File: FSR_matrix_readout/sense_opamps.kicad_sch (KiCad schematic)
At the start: 24 parts, among them U18 TLV9064, U19 TLV9064, U20 TLV9064, U3 TLV9064

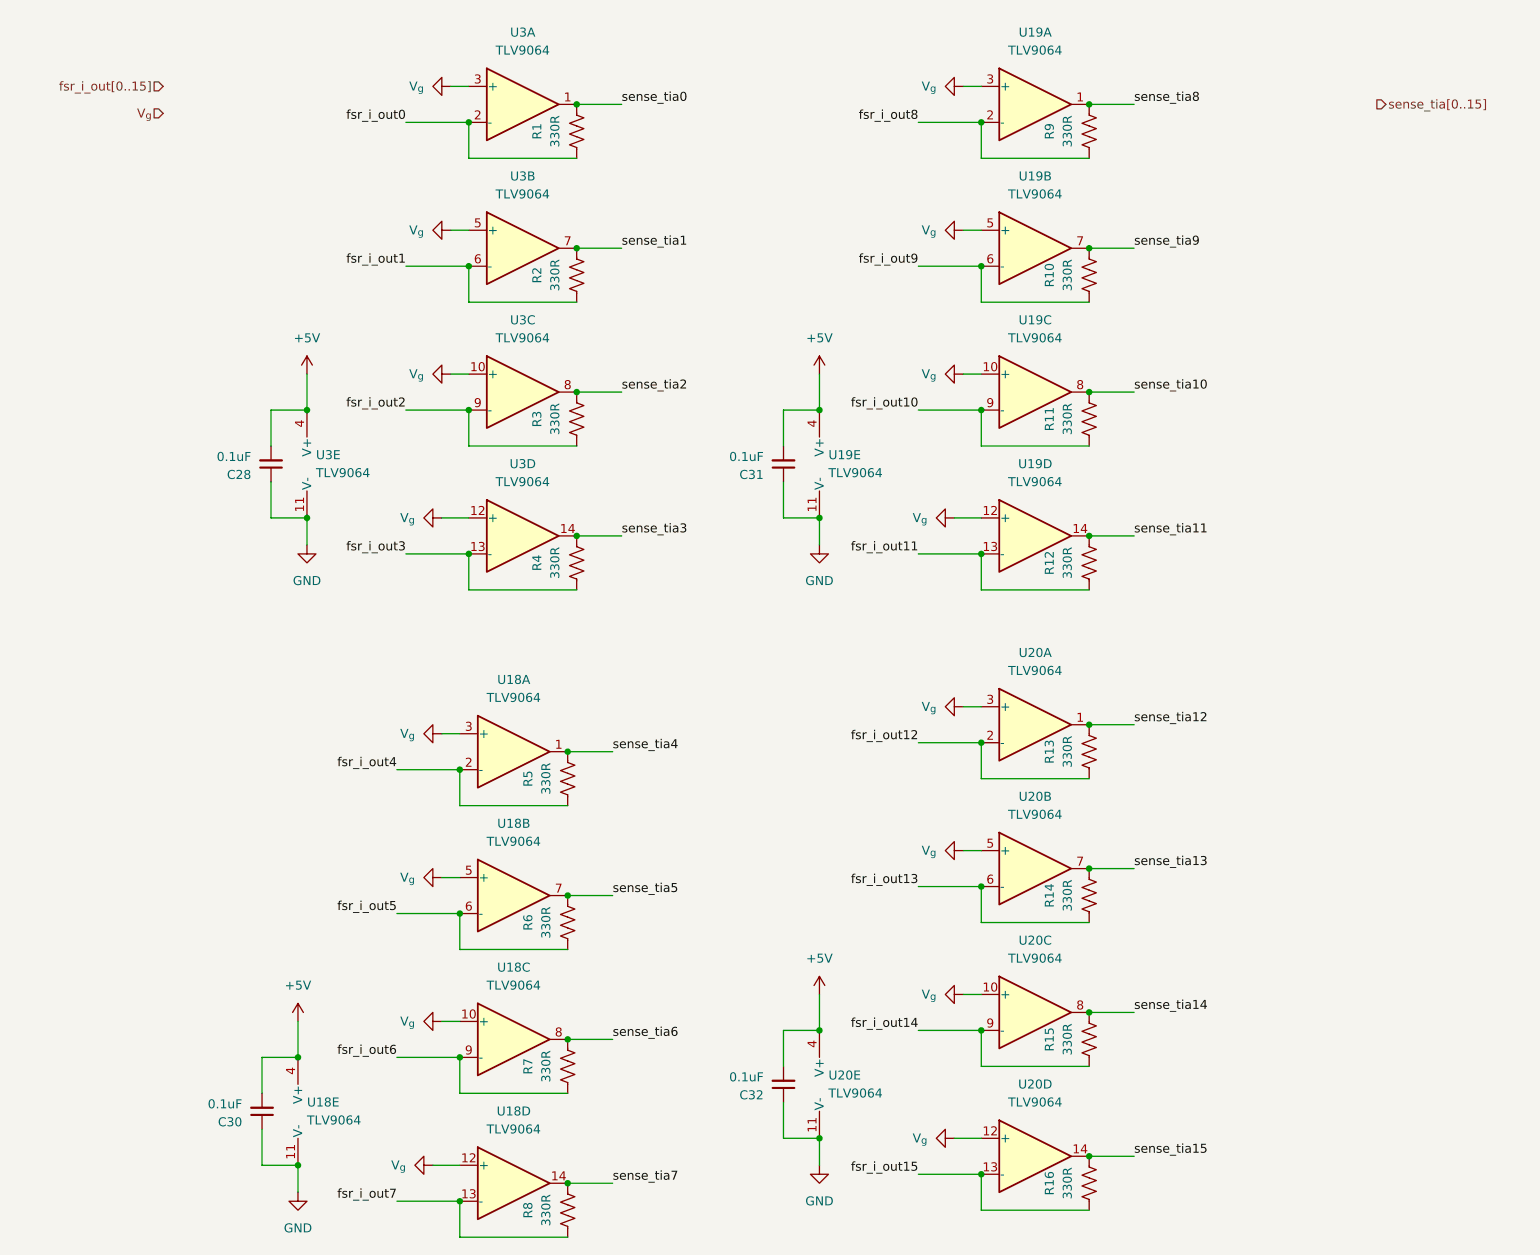
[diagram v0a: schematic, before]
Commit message: add feedback cap for TIA opamp
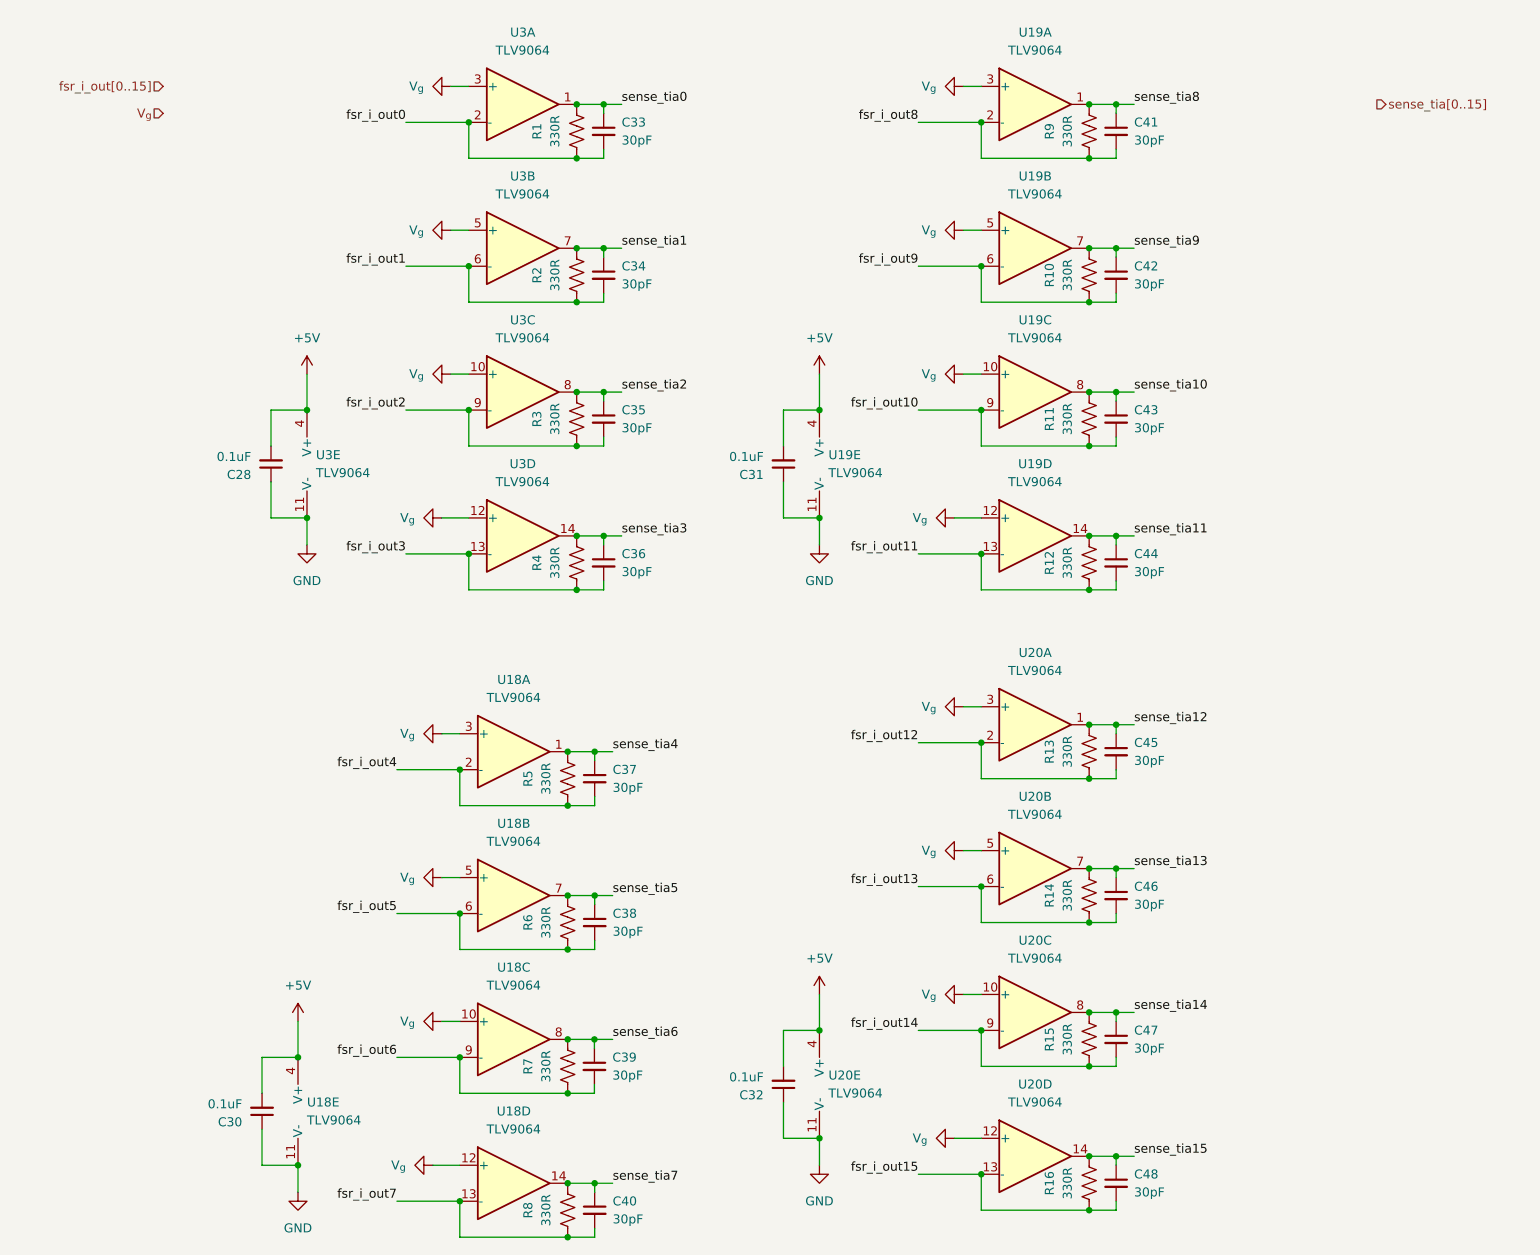
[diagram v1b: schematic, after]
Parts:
- added C33, C34, C35, C36, C37, C38, C39, C40, C41, C42, C43, C44, C45, C46, C47, C48: 30pF, symbol Device:C_Small
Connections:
- net fsr_i_out0: now also C33.2
- net fsr_i_out1: now also C34.2
- net fsr_i_out10: now also C43.2
- net fsr_i_out11: now also C44.2
- net fsr_i_out12: now also C45.2
- net fsr_i_out13: now also C46.2
- net fsr_i_out14: now also C47.2
- net fsr_i_out15: now also C48.2
- net fsr_i_out2: now also C35.2
- net fsr_i_out3: now also C36.2
- net fsr_i_out4: now also C37.2
- net fsr_i_out5: now also C38.2
- net fsr_i_out6: now also C39.2
- net fsr_i_out7: now also C40.2
- net fsr_i_out8: now also C41.2
- net fsr_i_out9: now also C42.2
- net sense_tia0: now also C33.1
- net sense_tia1: now also C34.1
- net sense_tia10: now also C43.1
- net sense_tia11: now also C44.1
- net sense_tia12: now also C45.1
- net sense_tia13: now also C46.1
- net sense_tia14: now also C47.1
- net sense_tia15: now also C48.1
- net sense_tia2: now also C35.1
- net sense_tia3: now also C36.1
- net sense_tia4: now also C37.1
- net sense_tia5: now also C38.1
- net sense_tia6: now also C39.1
- net sense_tia7: now also C40.1
- net sense_tia8: now also C41.1
- net sense_tia9: now also C42.1

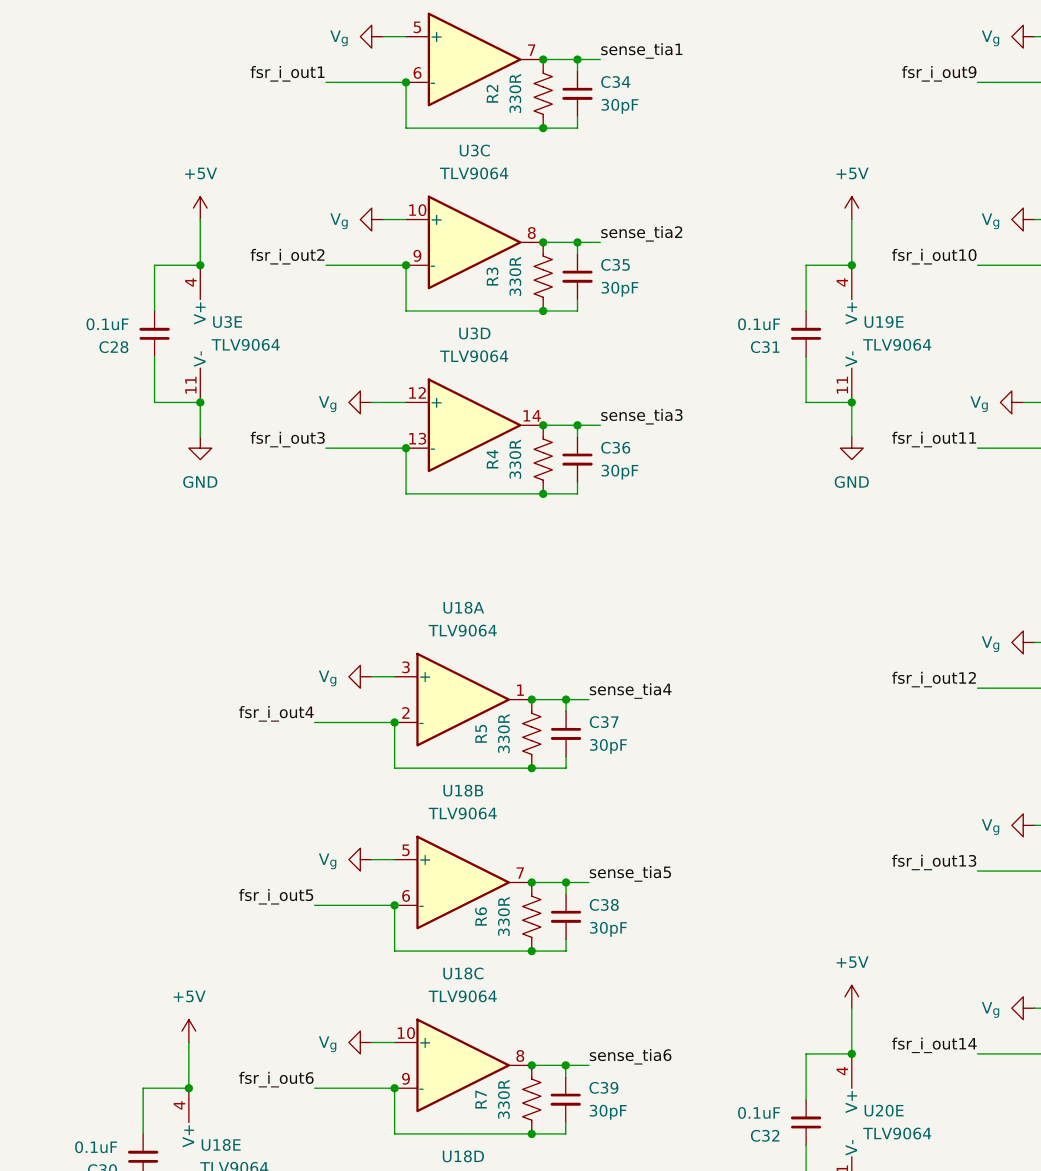
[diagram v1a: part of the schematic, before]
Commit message: done PGA and ADC
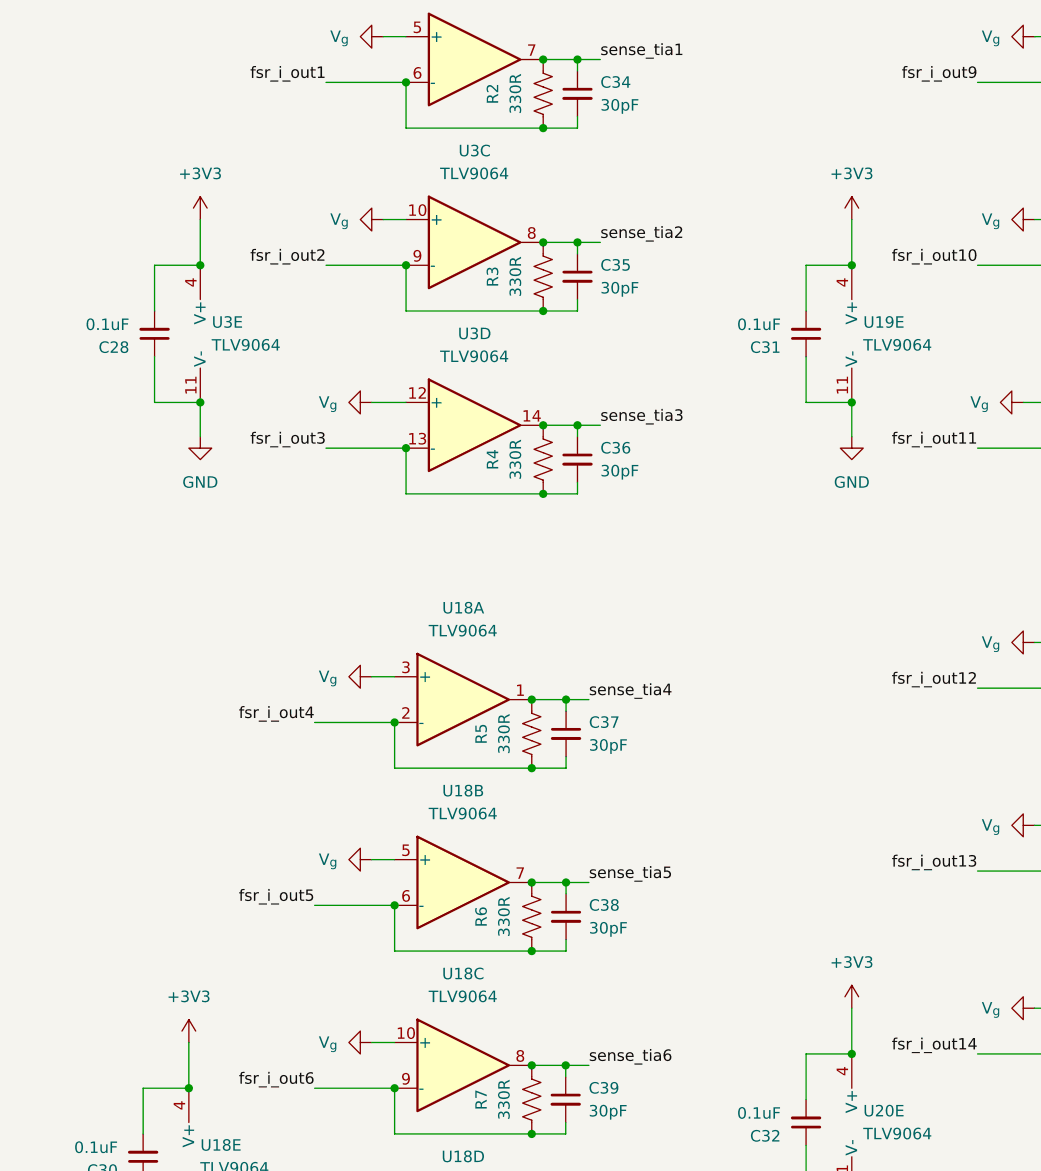
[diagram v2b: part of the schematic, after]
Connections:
- net +5V renamed +3V3

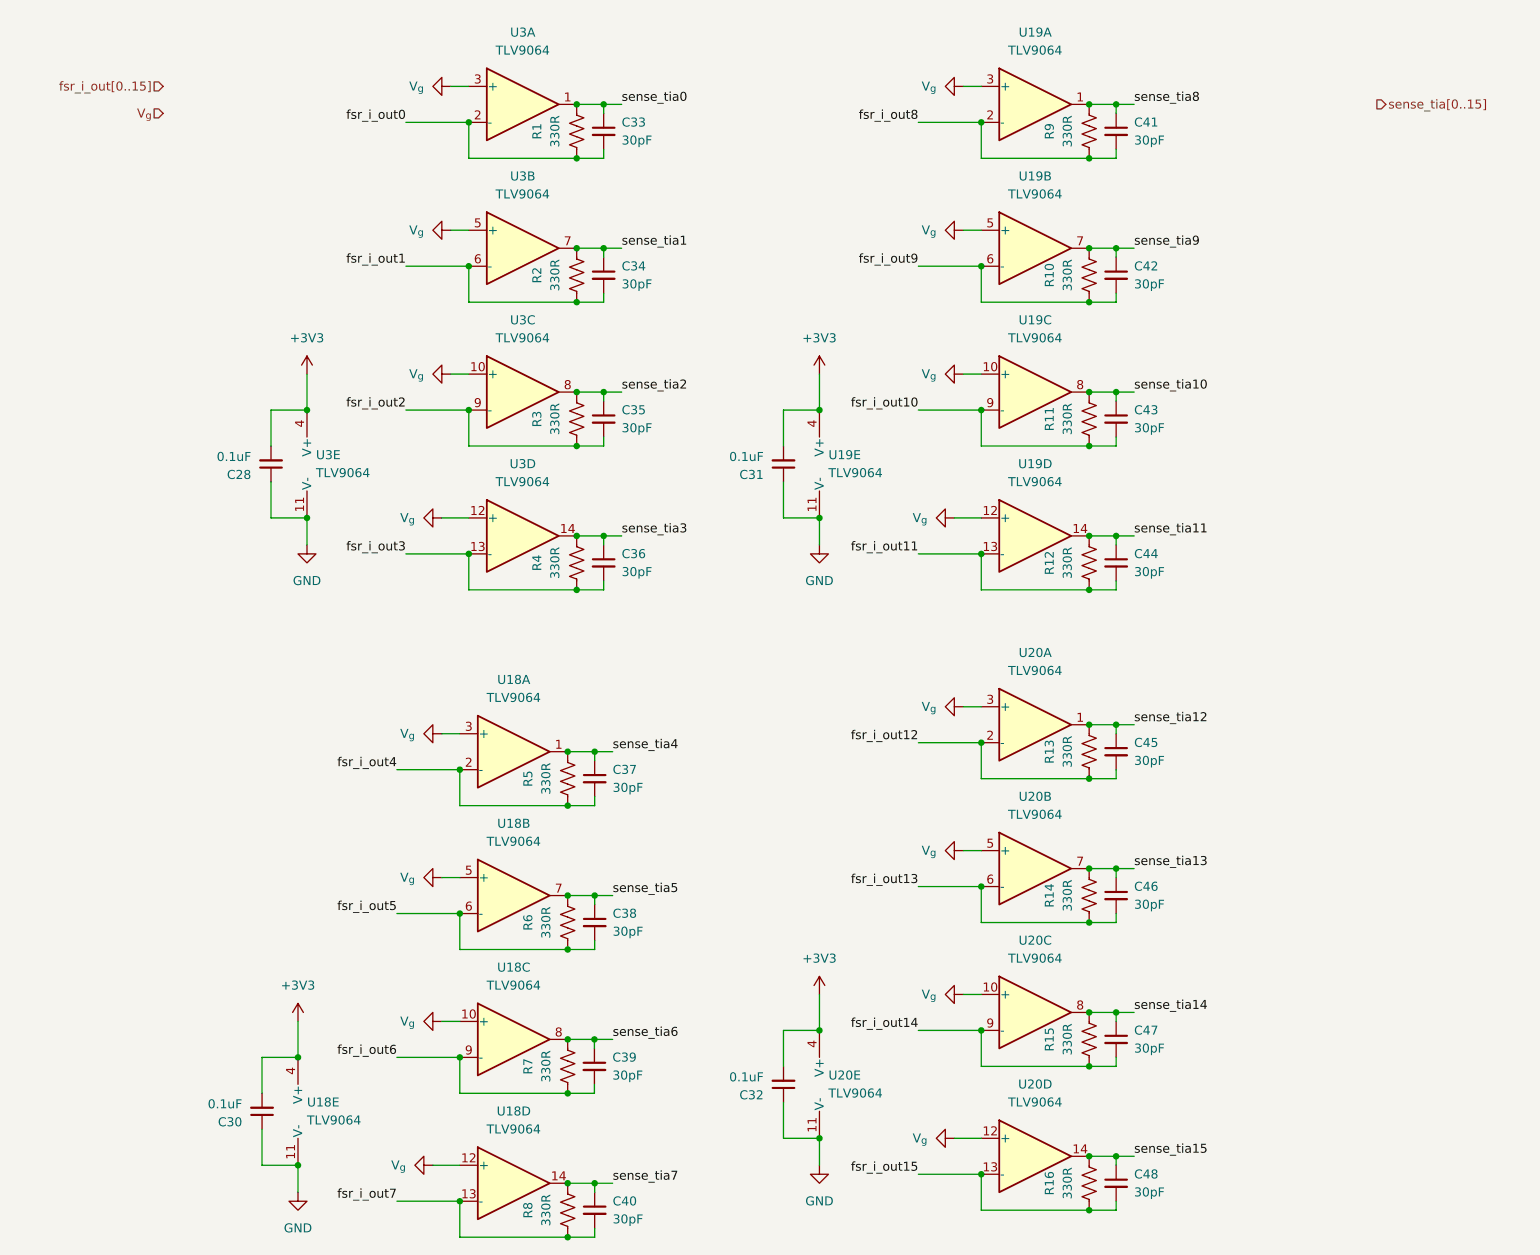
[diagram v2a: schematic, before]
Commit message: add decoupling cap for Vg in sense_opamps
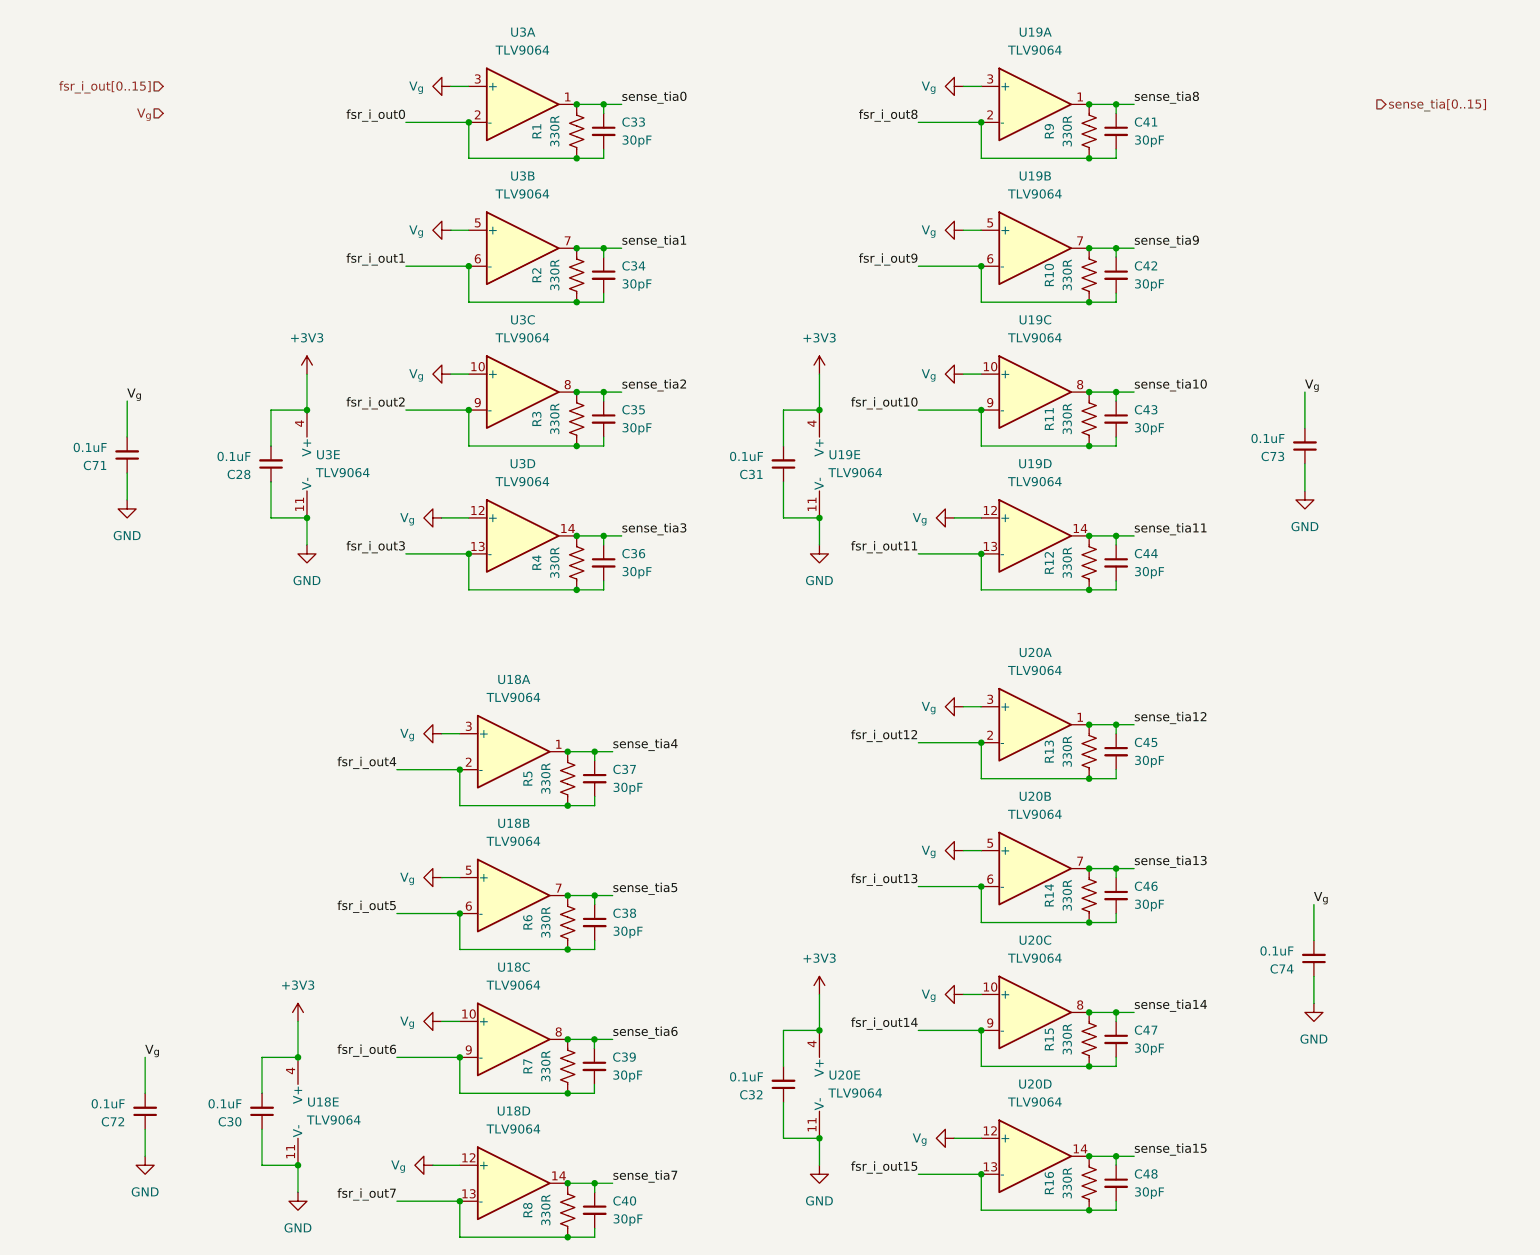
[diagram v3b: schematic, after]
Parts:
- added C71, C72, C73, C74: 0.1uF, symbol Device:C_Small
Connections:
- net GND: now also C71.1, C72.1, C73.1, C74.1
- net V_{g}: now also C71.2, C72.2, C73.2, C74.2
